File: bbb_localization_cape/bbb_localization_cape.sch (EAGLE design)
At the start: 33 parts, among them J2 MOLEX-22-03-5035, U1 SN65HVD256DR, U2 ARDUCAMOV5642, U3 SN74LV1T126DCKR, U4 MSP430G2553IPW20R, U5 SN74LV1T125DCKR, U6 LP38693MP-3.3/NOPB, U7 LM1085ISX-ADJ

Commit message: More or less finished with the schematic and layout
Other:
- note removed: "I2C2 - EEPROM Chip (Cape Standard) - Camera UART2_TXD - Dynamixel VDD_3V3EXP - Max current of 250mA - MCP2562 - 500uA - OV5642 - ~270mA Tri-State Buffer - P9.23"
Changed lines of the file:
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@@
 <description>Main</description>
 <plain>
-<text x="137.16" y="165.1" size="1.778" layer="97">I2C2
-- EEPROM Chip (Cape Standard)
-- Camera
-UART2_TXD
-- Dynamixel
-VDD_3V3EXP
-- Max current of 250mA
-  - MCP2562 - 500uA
-  - OV5642 - ~270mA
-Tri-State Buffer
-- P9.23
-</text>
 </plain>
 <instances>
@@
 </drawing>
 <compatibility>
-<note version="6.3" minversion="6.2.2" severity="warning">
-Since Version 6.2.2 text objects can contain more than one line,
-which will not be processed correctly with this version.
-</note>
 <note version="8.2" severity="warning">
 Since Version 8.2, EAGLE supports online libraries. The ids

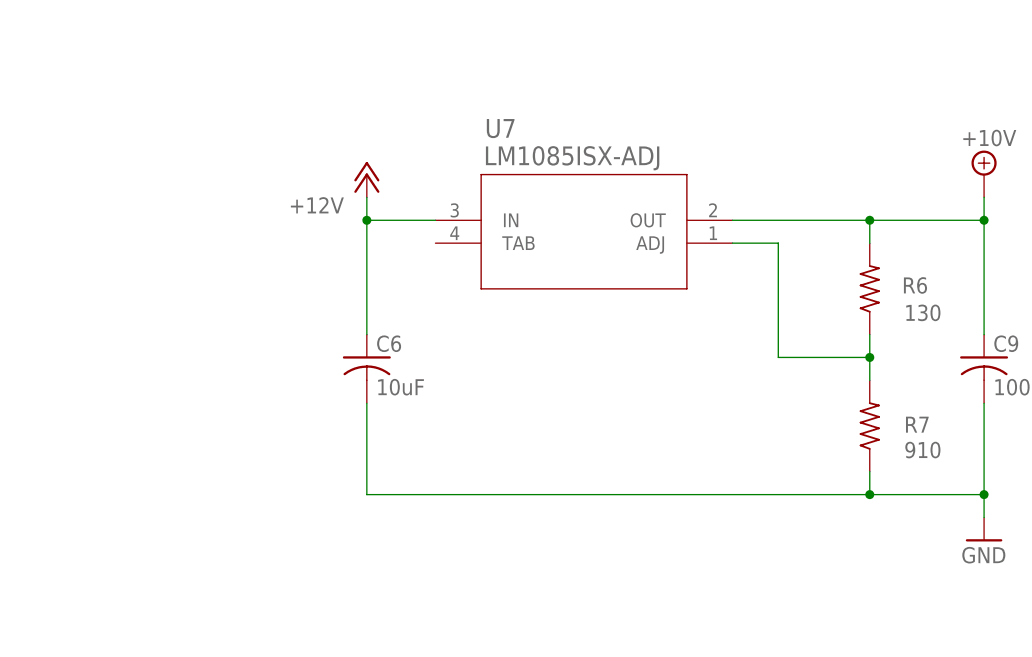
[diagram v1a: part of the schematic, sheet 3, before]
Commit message: Laid out power connections
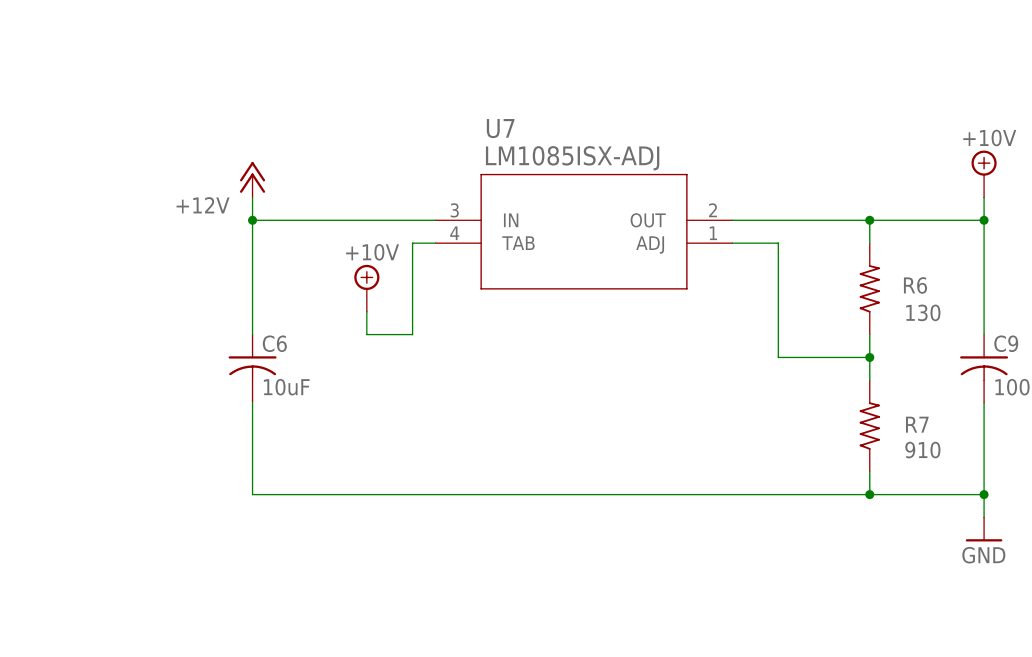
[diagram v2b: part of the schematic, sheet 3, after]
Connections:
- net +10V: now also U7.TAB
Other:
- moved on the sheet: C6
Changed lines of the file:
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@@
 <setting verticaltext="up"/>
 </settings>
-<grid distance="0.1" unitdist="inch" unit="inch" style="lines" multiple="1" display="yes" altdistance="0.01" altunitdist="inch" altunit="inch"/>
+<grid distance="0.1" unitdist="inch" unit="mm" style="lines" multiple="1" display="yes" altdistance="0.01" altunitdist="inch" altunit="inch"/>
 <layers>
 <layer number="1" name="Top" color="4" fill="1" visible="no" active="no"/>
@@
 <part name="GND4" library="supply1" library_urn="urn:adsk.eagle:library:371" deviceset="GND" device=""/>
 <part name="FRAME2" library="frames" library_urn="urn:adsk.eagle:library:229" deviceset="FRAME_A_L" device=""/>
+<part name="SUPPLY3" library="supply2" library_urn="urn:adsk.eagle:library:372" deviceset="+10V" device=""/>
 </parts>
 <sheets>
@@
 <attribute name="VALUE" x="83.82" y="165.1" size="1.778" layer="96"/>
 </instance>
-<instance part="P+9" gate="1" x="157.48" y="104.14" smashed="yes">
-<attribute name="VALUE" x="154.94" y="101.6" size="1.778" layer="96" rot="R180"/>
+<instance part="P+9" gate="1" x="144.78" y="104.14" smashed="yes">
+<attribute name="VALUE" x="142.24" y="101.6" size="1.778" layer="96" rot="R180"/>
 </instance>
 <instance part="SUPPLY2" gate="G$1" x="226.06" y="104.14"/>
@@
 <instance part="C5" gate="G$1" x="96.52" y="66.04"/>
 <instance part="C9" gate="G$1" x="226.06" y="83.82"/>
-<instance part="C6" gate="G$1" x="157.48" y="83.82"/>
+<instance part="C6" gate="G$1" x="144.78" y="83.82"/>
 <instance part="C3" gate="G$1" x="50.8" y="66.04"/>
 <instance part="GND10" gate="1" x="96.52" y="50.8"/>
 <instance part="FRAME3" gate="G$1" x="0" y="0"/>
 <instance part="FRAME3" gate="G$2" x="172.72" y="0"/>
+<instance part="SUPPLY3" gate="G$1" x="157.48" y="91.44"/>
 </instances>
 <busses>
@@
 <junction x="226.06" y="68.58"/>
 <pinref part="C6" gate="G$1" pin="2"/>
-<wire x1="157.48" y1="78.74" x2="157.48" y2="68.58" width="0.1524" layer="91"/>
-<wire x1="157.48" y1="68.58" x2="213.36" y2="68.58" width="0.1524" layer="91"/>
+<wire x1="144.78" y1="78.74" x2="144.78" y2="68.58" width="0.1524" layer="91"/>
+<wire x1="144.78" y1="68.58" x2="213.36" y2="68.58" width="0.1524" layer="91"/>
 <junction x="213.36" y="68.58"/>
 </segment>
@@
 <segment>
 <pinref part="P+9" gate="1" pin="+12V"/>
-<wire x1="157.48" y1="101.6" x2="157.48" y2="99.06" width="0.1524" layer="91"/>
+<wire x1="144.78" y1="101.6" x2="144.78" y2="99.06" width="0.1524" layer="91"/>
 <pinref part="U7" gate="A" pin="IN"/>
-<wire x1="165.1" y1="99.06" x2="157.48" y2="99.06" width="0.1524" layer="91"/>
+<wire x1="165.1" y1="99.06" x2="144.78" y2="99.06" width="0.1524" layer="91"/>
 <pinref part="C6" gate="G$1" pin="1"/>
-<wire x1="157.48" y1="86.36" x2="157.48" y2="99.06" width="0.1524" layer="91"/>
-<junction x="157.48" y="99.06"/>
+<wire x1="144.78" y1="86.36" x2="144.78" y2="99.06" width="0.1524" layer="91"/>
+<junction x="144.78" y="99.06"/>
 </segment>
 <segment>
@@
 <junction x="226.06" y="99.06"/>
 </segment>
-</net>
+<segment>
+<pinref part="SUPPLY3" gate="G$1" pin="+10V"/>
+<wire x1="157.48" y1="88.9" x2="157.48" y2="86.36" width="0.1524" layer="91"/>
+<wire x1="157.48" y1="86.36" x2="162.56" y2="86.36" width="0.1524" layer="91"/>
+<pinref part="U7" gate="A" pin="TAB"/>
+<wire x1="165.1" y1="96.52" x2="162.56" y2="96.52" width="0.1524" layer="91"/>
+<wire x1="162.56" y1="86.36" x2="162.56" y2="96.52" width="0.1524" layer="91"/>
+</segment>
+</net>

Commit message: Fixed issues between board and schematic, had to ripup the board
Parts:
- renumbered PAD1 to +12V, PAD2 to GND
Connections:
- removed net I2C2_SCL: A1.I2C2_SCL, R1.1, U2.SCL
- net I2C_SCL: now also A1.I2C2_SCL, R1.1, U2.SCL
- net PRU1_12: now also A1.GPIO1_30
- net UART2_DIR: now also A1.GPIO1_17
- net UART_MSP_DIR: now also U4.P2.0/TA1.0

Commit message: Cleaned up beaglebone_outline schematic symbol
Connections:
- removed net I2C_SCL: A1.I2C2_SCL, R1.1, U2.SCL, U4.P1.6/TA0.1/UCB0SOMI/UCB0SCL/A6/CA6/TDI/TCLK
- removed net I2C_SDA: A1.I2C2_SDA, R2.1, U2.SDATA, U4.P1.7/CAOUT/UCB0SIMO/UCB0SDA/A7/CA7/TDO/TDI
- new net I2C2_SCL: A1.19@P9, R1.1, U2.SCL, U4.P1.6/TA0.1/UCB0SOMI/UCB0SCL/A6/CA6/TDI/TCLK
- new net I2C2_SDA: A1.20@P9, R2.1, U2.SDATA, U4.P1.7/CAOUT/UCB0SIMO/UCB0SDA/A7/CA7/TDO/TDI
- net +5V: now also A1.05.VDD_5V@P9, A1.VDD_5V.06@P9; no longer A1.VDD_5V@1, A1.VDD_5V@2
- net DCAN1_RX: now also A1.24@P9; no longer A1.UART1_TXD
- net DCAN1_TX: now also A1.26@P9; no longer A1.UART1_RXD
- net GND: now also A1.01.DGND@P8, A1.01.DGND@P9, A1.43.DGND@P9, A1.45.DGND@P9, A1.DGND.02@P8, A1.DGND.44@P9, A1.DGND.46@P9, A1.GND.02@P9; no longer A1.GND@1, A1.GND@2
- net PRU1_0: now also A1.45@P8; no longer A1.GPIO2_6
- net PRU1_1: now also A1.46@P8; no longer A1.GPIO2_7
- net PRU1_10: now also A1.28@P8; no longer A1.GPIO2_24
- net PRU1_11: now also A1.30@P8; no longer A1.GPIO2_25
- net PRU1_12: now also A1.21@P8; no longer A1.GPIO1_30
- net PRU1_2: now also A1.43@P8; no longer A1.GPIO2_8
- net PRU1_3: now also A1.44@P8; no longer A1.GPIO2_9
- net PRU1_4: now also A1.41@P8; no longer A1.GPIO2_10
- net PRU1_5: now also A1.42@P8; no longer A1.GPIO2_11
- net PRU1_6: now also A1.39@P8; no longer A1.GPIO2_12
- net PRU1_7: now also A1.40@P8; no longer A1.GPIO2_13
- net PRU1_8: now also A1.27@P8; no longer A1.GPIO2_22
- net PRU1_9: now also A1.29@P8; no longer A1.GPIO2_23
- net PWDN: now also A1.25@P8; no longer A1.GPIO1_0
- net TIMER4: now also A1.07@P8; no longer A1.TIMER4
- net UART2_DIR: now also A1.23@P9; no longer A1.GPIO1_17
- net UART2_RXD: now also A1.22@P9; no longer A1.UART2_RXD
- net UART2_TXD: now also A1.21@P9; no longer A1.UART2_TXD
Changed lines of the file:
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@@
 <setting verticaltext="up"/>
 </settings>
-<grid distance="0.1" unitdist="inch" unit="inch" style="lines" multiple="1" display="no" altdistance="0.01" altunitdist="inch" altunit="inch"/>
+<grid distance="0.1" unitdist="inch" unit="inch" style="lines" multiple="1" display="yes" altdistance="0.01" altunitdist="inch" altunit="inch"/>
 <layers>
 <layer number="1" name="Top" color="4" fill="1" visible="no" active="no"/>
@@
 <net name="+5V" class="0">
 <segment>
-<pinref part="A1" gate="G$1" pin="VDD_5V@1"/>
+<pinref part="A1" gate="G$1" pin="05.VDD_5V@P9"/>
 <wire x1="53.34" y1="116.84" x2="33.02" y2="116.84" width="0.1524" layer="91"/>
 <label x="33.02" y="116.84" size="1.778" layer="95"/>
 </segment>
 <segment>
-<pinref part="A1" gate="G$1" pin="VDD_5V@2"/>
+<pinref part="A1" gate="G$1" pin="VDD_5V.06@P9"/>
 <wire x1="109.22" y1="116.84" x2="129.54" y2="116.84" width="0.1524" layer="91"/>
 <label x="129.54" y="116.84" size="1.778" layer="95" rot="MR0"/>
@@
 <net name="GND" class="0">
 <segment>
-<pinref part="A1" gate="G$1" pin="GND@1"/>
+<pinref part="A1" gate="G$1" pin="01.DGND@P9"/>
 <wire x1="53.34" y1="121.92" x2="33.02" y2="121.92" width="0.1524" layer="91"/>
 <label x="33.02" y="121.92" size="1.778" layer="95"/>
 </segment>
 <segment>
-<pinref part="A1" gate="G$1" pin="GND@2"/>
+<pinref part="A1" gate="G$1" pin="GND.02@P9"/>
 <wire x1="109.22" y1="121.92" x2="129.54" y2="121.92" width="0.1524" layer="91"/>
 <label x="129.54" y="121.92" size="1.778" layer="95" rot="MR0"/>
@@
 <label x="246.38" y="68.58" size="1.778" layer="95" rot="MR0"/>
 </segment>
+<segment>
+<pinref part="A1" gate="G$1" pin="01.DGND@P8"/>
+<wire x1="53.34" y1="187.96" x2="33.02" y2="187.96" width="0.1524" layer="91"/>
+<label x="33.02" y="187.96" size="1.778" layer="95"/>
+</segment>
+<segment>
+<pinref part="A1" gate="G$1" pin="DGND.02@P8"/>
+<wire x1="109.22" y1="187.96" x2="129.54" y2="187.96" width="0.1524" layer="91"/>
+<label x="129.54" y="187.96" size="1.778" layer="95" rot="MR0"/>
+</segment>
+<segment>
+<pinref part="A1" gate="G$1" pin="43.DGND@P9"/>
+<wire x1="53.34" y1="68.58" x2="33.02" y2="68.58" width="0.1524" layer="91"/>
+<label x="33.02" y="68.58" size="1.778" layer="95"/>
+</segment>
+<segment>
+<pinref part="A1" gate="G$1" pin="45.DGND@P9"/>
+<wire x1="53.34" y1="66.04" x2="33.02" y2="66.04" width="0.1524" layer="91"/>
+<label x="33.02" y="66.04" size="1.778" layer="95"/>
+</segment>
+<segment>
+<pinref part="A1" gate="G$1" pin="DGND.44@P9"/>
+<wire x1="109.22" y1="68.58" x2="129.54" y2="68.58" width="0.1524" layer="91"/>
+<label x="129.54" y="68.58" size="1.778" layer="95" rot="MR0"/>
+</segment>
+<segment>
+<pinref part="A1" gate="G$1" pin="DGND.46@P9"/>
+<wire x1="109.22" y1="66.04" x2="129.54" y2="66.04" width="0.1524" layer="91"/>
+<label x="129.54" y="66.04" size="1.778" layer="95" rot="MR0"/>
+</segment>
 </net>
 <net name="DCAN1_RX" class="0">
 <segment>
-<pinref part="A1" gate="G$1" pin="UART1_TXD"/>
+<pinref part="A1" gate="G$1" pin="24@P9"/>
 <wire x1="109.22" y1="93.98" x2="129.54" y2="93.98" width="0.1524" layer="91"/>
 <label x="129.54" y="93.98" size="1.778" layer="95" rot="MR0"/>
@@
 <net name="DCAN1_TX" class="0">
 <segment>
-<pinref part="A1" gate="G$1" pin="UART1_RXD"/>
+<pinref part="A1" gate="G$1" pin="26@P9"/>
 <wire x1="109.22" y1="91.44" x2="129.54" y2="91.44" width="0.1524" layer="91"/>
 <label x="129.54" y="91.44" size="1.778" layer="95" rot="MR0"/>
@@
 </segment>
 </net>
-<net name="I2C_SDA" class="0">
-<segment>
-<pinref part="A1" gate="G$1" pin="I2C2_SDA"/>
+<net name="I2C2_SDA" class="0">
+<segment>
+<pinref part="A1" gate="G$1" pin="20@P9"/>
 <wire x1="109.22" y1="99.06" x2="129.54" y2="99.06" width="0.1524" layer="91"/>
 <label x="129.54" y="99.06" size="1.778" layer="95" rot="MR0"/>
@@
 <net name="UART2_RXD" class="0">
 <segment>
-<pinref part="A1" gate="G$1" pin="UART2_RXD"/>
+<pinref part="A1" gate="G$1" pin="22@P9"/>
 <wire x1="109.22" y1="96.52" x2="129.54" y2="96.52" width="0.1524" layer="91"/>
 <label x="129.54" y="96.52" size="1.778" layer="95" rot="MR0"/>
@@
 <net name="UART2_TXD" class="0">
 <segment>
-<pinref part="A1" gate="G$1" pin="UART2_TXD"/>
+<pinref part="A1" gate="G$1" pin="21@P9"/>
 <wire x1="53.34" y1="96.52" x2="33.02" y2="96.52" width="0.1524" layer="91"/>
 <label x="33.02" y="96.52" size="1.778" layer="95"/>
@@
 <net name="PRU1_1" class="0">
 <segment>
-<pinref part="A1" gate="G$1" pin="GPIO2_7"/>
+<pinref part="A1" gate="G$1" pin="46@P8"/>
 <wire x1="109.22" y1="132.08" x2="129.54" y2="132.08" width="0.1524" layer="91"/>
 <label x="129.54" y="132.08" size="1.778" layer="95" rot="MR0"/>
@@
 <net name="PRU1_3" class="0">
 <segment>
-<pinref part="A1" gate="G$1" pin="GPIO2_9"/>
+<pinref part="A1" gate="G$1" pin="44@P8"/>
 <wire x1="109.22" y1="134.62" x2="129.54" y2="134.62" width="0.1524" layer="91"/>
 <label x="129.54" y="134.62" size="1.778" layer="95" rot="MR0"/>
@@
 <net name="PRU1_5" class="0">
 <segment>
-<pinref part="A1" gate="G$1" pin="GPIO2_11"/>
+<pinref part="A1" gate="G$1" pin="42@P8"/>
 <wire x1="109.22" y1="137.16" x2="129.54" y2="137.16" width="0.1524" layer="91"/>
 <label x="129.54" y="137.16" size="1.778" layer="95" rot="MR0"/>
@@
 <net name="PRU1_7" class="0">
 <segment>
-<pinref part="A1" gate="G$1" pin="GPIO2_13"/>
+<pinref part="A1" gate="G$1" pin="40@P8"/>
 <wire x1="109.22" y1="139.7" x2="129.54" y2="139.7" width="0.1524" layer="91"/>
 <label x="129.54" y="139.7" size="1.778" layer="95" rot="MR0"/>
@@
 <net name="PRU1_0" class="0">
 <segment>
-<pinref part="A1" gate="G$1" pin="GPIO2_6"/>
+<pinref part="A1" gate="G$1" pin="45@P8"/>
 <wire x1="53.34" y1="132.08" x2="33.02" y2="132.08" width="0.1524" layer="91"/>
 <label x="33.02" y="132.08" size="1.778" layer="95"/>
@@
 <net name="PRU1_2" class="0">
 <segment>
-<pinref part="A1" gate="G$1" pin="GPIO2_8"/>
+<pinref part="A1" gate="G$1" pin="43@P8"/>
 <wire x1="53.34" y1="134.62" x2="33.02" y2="134.62" width="0.1524" layer="91"/>
 <label x="33.02" y="134.62" size="1.778" layer="95"/>
@@
 <net name="PRU1_4" class="0">
 <segment>
-<pinref part="A1" gate="G$1" pin="GPIO2_10"/>
+<pinref part="A1" gate="G$1" pin="41@P8"/>
 <wire x1="53.34" y1="137.16" x2="33.02" y2="137.16" width="0.1524" layer="91"/>
 <label x="33.02" y="137.16" size="1.778" layer="95"/>
@@
 <net name="PRU1_6" class="0">
 <segment>
-<pinref part="A1" gate="G$1" pin="GPIO2_12"/>
+<pinref part="A1" gate="G$1" pin="39@P8"/>
 <wire x1="53.34" y1="139.7" x2="33.02" y2="139.7" width="0.1524" layer="91"/>
 <label x="33.02" y="139.7" size="1.778" layer="95"/>
@@
 <net name="PRU1_9" class="0">
 <segment>
-<pinref part="A1" gate="G$1" pin="GPIO2_23"/>
+<pinref part="A1" gate="G$1" pin="29@P8"/>
 <wire x1="53.34" y1="152.4" x2="33.02" y2="152.4" width="0.1524" layer="91"/>
 <label x="33.02" y="152.4" size="1.778" layer="95"/>
@@
 <net name="PRU1_8" class="0">
 <segment>
-<pinref part="A1" gate="G$1" pin="GPIO2_22"/>
+<pinref part="A1" gate="G$1" pin="27@P8"/>
 <wire x1="53.34" y1="154.94" x2="33.02" y2="154.94" width="0.1524" layer="91"/>
 <label x="33.02" y="154.94" size="1.778" layer="95"/>
@@
 <net name="PRU1_11" class="0">
 <segment>
-<pinref part="A1" gate="G$1" pin="GPIO2_25"/>
+<pinref part="A1" gate="G$1" pin="30@P8"/>
 <wire x1="109.22" y1="152.4" x2="129.54" y2="152.4" width="0.1524" layer="91"/>
 <label x="129.54" y="152.4" size="1.778" layer="95" rot="MR0"/>
@@
 <net name="PRU1_10" class="0">
 <segment>
-<pinref part="A1" gate="G$1" pin="GPIO2_24"/>
+<pinref part="A1" gate="G$1" pin="28@P8"/>
 <wire x1="109.22" y1="154.94" x2="129.54" y2="154.94" width="0.1524" layer="91"/>
 <label x="129.54" y="154.94" size="1.778" layer="95" rot="MR0"/>
@@
 <net name="TIMER4" class="0">
 <segment>
-<pinref part="A1" gate="G$1" pin="TIMER4"/>
+<pinref part="A1" gate="G$1" pin="07@P8"/>
 <wire x1="53.34" y1="180.34" x2="33.02" y2="180.34" width="0.1524" layer="91"/>
 <label x="33.02" y="180.34" size="1.778" layer="95"/>
@@
 <net name="PWDN" class="0">
 <segment>
-<pinref part="A1" gate="G$1" pin="GPIO1_0"/>
+<pinref part="A1" gate="G$1" pin="25@P8"/>
 <wire x1="53.34" y1="157.48" x2="33.02" y2="157.48" width="0.1524" layer="91"/>
 <label x="33.02" y="157.48" size="1.778" layer="95"/>
@@
 </segment>
 <segment>
-<pinref part="A1" gate="G$1" pin="GPIO1_30"/>
+<pinref part="A1" gate="G$1" pin="21@P8"/>
 <wire x1="53.34" y1="162.56" x2="33.02" y2="162.56" width="0.1524" layer="91"/>
 <label x="33.02" y="162.56" size="1.778" layer="95"/>
@@
 </segment>
 <segment>
-<pinref part="A1" gate="G$1" pin="GPIO1_17"/>
+<pinref part="A1" gate="G$1" pin="23@P9"/>
 <wire x1="53.34" y1="93.98" x2="33.02" y2="93.98" width="0.1524" layer="91"/>
 <label x="33.02" y="93.98" size="1.778" layer="95"/>
 </segment>
 </net>
-<net name="I2C_SCL" class="0">
-<segment>
-<pinref part="A1" gate="G$1" pin="I2C2_SCL"/>
+<net name="I2C2_SCL" class="0">
+<segment>
+<pinref part="A1" gate="G$1" pin="19@P9"/>
 <wire x1="53.34" y1="99.06" x2="33.02" y2="99.06" width="0.1524" layer="91"/>
 <label x="33.02" y="99.06" size="1.778" layer="95"/>
@@
 </segment>
 </net>
-<net name="I2C_SDA" class="0">
+<net name="I2C2_SDA" class="0">
 <segment>
 <pinref part="U4" gate="A" pin="P1.7/CAOUT/UCB0SIMO/UCB0SDA/A7/CA7/TDO/TDI"/>
@@
 </segment>
 </net>
-<net name="I2C_SCL" class="0">
+<net name="I2C2_SCL" class="0">
 <segment>
 <pinref part="U4" gate="A" pin="P1.6/TA0.1/UCB0SOMI/UCB0SCL/A6/CA6/TDI/TCLK"/>
